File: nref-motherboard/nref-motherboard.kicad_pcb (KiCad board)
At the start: 6 copper layers, 122.6 x 80 mm, 204 parts, among them J1 POWSW, J10 DISP, J11 BAT1, J12 BAT2, J13 SYSCTL_USB, J16 Conn_01x10_Pin, J17 Conn_01x10_Pin, J18 Conn_01x20, J19 SER, J2 Conn_01x12_Pin, J4 1-2199230-6, J5 SYSCTL, J6 USB_INT1, J7 PWR, J8 Conn_01x12_Pin, J9 Conn_01x14_Pin, Q1 NTMFD6H840NL, Q2 NTMFD6H840NL, SW2 RESET, SW4 SW_DIP_x08, U1 reform2-som-connector, U10 BQ25756RRVR, U11 LM62460, U2 74HC573, U3 MAX1837EUT33+T, U5 LM62460, U7 USB2514B_Bi, U8 RP2040, U9 W25Q32JVSS, Y1 12MHz 18pF, Y2 24MHz

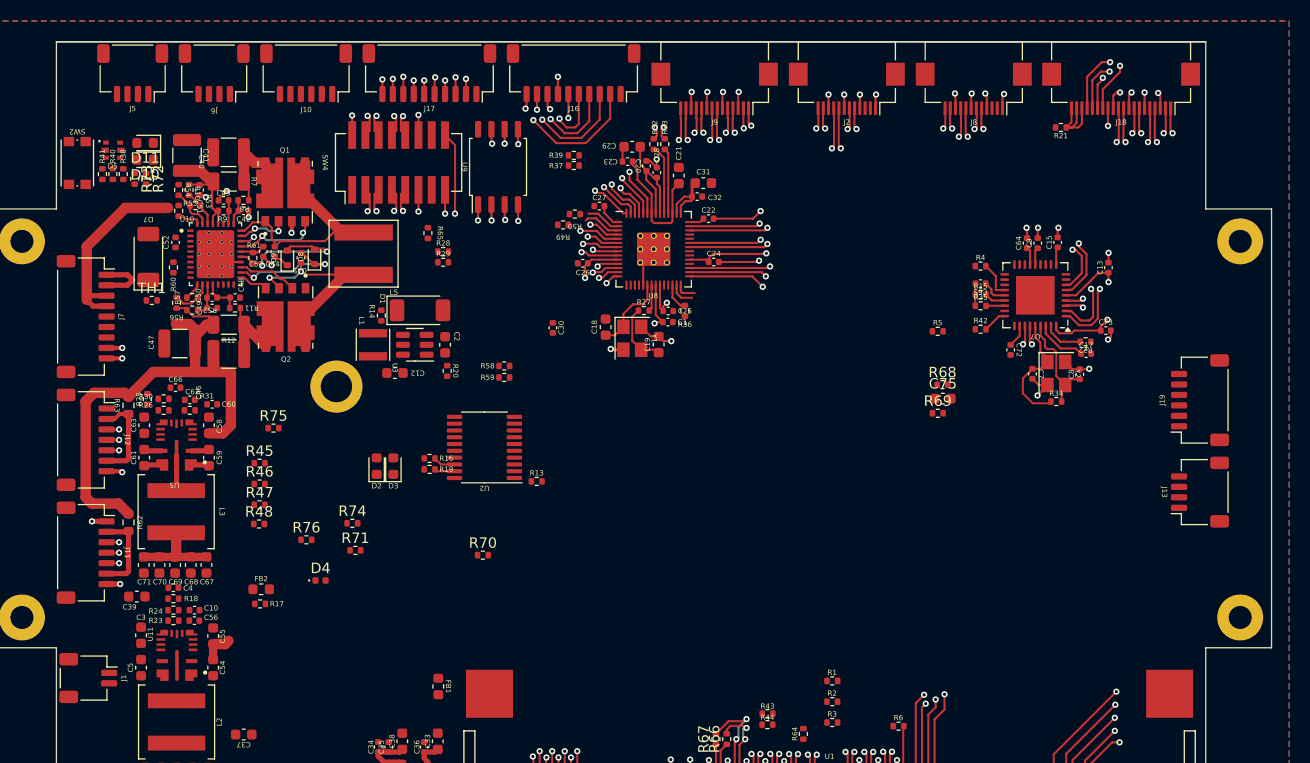
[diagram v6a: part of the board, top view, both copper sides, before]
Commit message: mb: swap some intersecting connectors; more routing
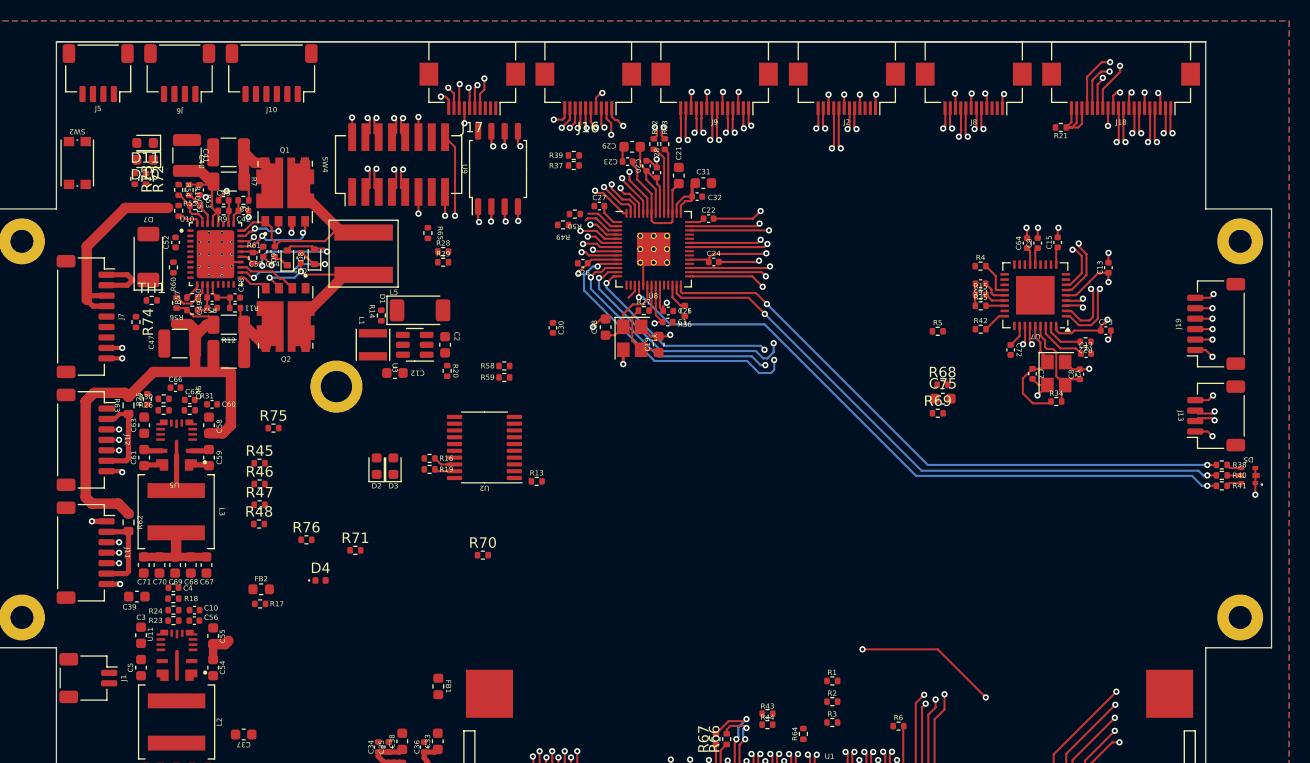
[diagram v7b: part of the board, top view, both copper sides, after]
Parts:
- J16, J17: footprint Connector_JST:JST_SH_SM10B-SRSS-TB_1x10-1MP_P1.00mm_Horizontal -> Connector_FFC-FPC:Hirose_FH12-10S-0.5SH_1x10-1MP_P0.50mm_Horizontal
- moved D5 113.0 mm to (144.1, 141.5), turned to 180 degrees
- moved R41 111.2 mm to (141.5, 142.5), turned to 0 degrees
- moved R40 110.0 mm to (141.5, 141.5), turned to 0 degrees
- moved R38 108.8 mm to (141.5, 140.5), turned to 0 degrees
- moved R74 28.3 mm to (37.6, 126.8), turned to -90 degrees
- moved J19 7.46 mm to (141.0, 127.0)
- moved J13 7.46 mm to (141.0, 135.8)
- moved J17 4.37 mm to (69.8, 104.5)
- moved J6 3.30 mm to (41.8, 103.0)
- moved J10 3.30 mm to (50.6, 103.0)
- moved J5 3.30 mm to (34.0, 103.0)
- moved J16 2.05 mm to (80.9, 104.5)
- moved SW4 0.20 mm to (62.8, 111.8)
- moved U9 0.20 mm to (72.3, 112.2)
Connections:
- J16 pad 2: SD_D0 -> SD_DET
- J16 pad 3: SD_D1 -> SD_CLK
- J16 pad 4: SD_D2 -> GND
- J16 pad 5: SD_D3 -> SD_CMD
- J16 pad 6: SD_CMD -> SD_D3
- J16 pad 7: GND -> SD_D2
- J16 pad 8: SD_CLK -> SD_D1
- J16 pad 9: SD_DET -> SD_D0
- U1 pad 30: RP_UART2_RX -> unconnected-(U1-UART3_TXD-Pad30)
- U1 pad 32: RP_UART2_TX -> unconnected-(U1-UART3_RXD-Pad32)
- U8 pad 15: RP_UART2_TX -> unconnected-(U8-GPIO12-Pad15)
- U8 pad 16: RP_UART2_RX -> unconnected-(U8-GPIO13-Pad16)
- U8 pad 35: 1V1_ENABLE -> unconnected-(U8-GPIO23-Pad35)
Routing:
- net IMX_WAKE: track 9.47 -> 76.8 mm, vias 2 -> 4
- net LPC_MOSI: track 14.2 -> 78.5 mm, vias 2 -> 3
- net Net-(U8-GPIO15): track 0.00 -> 63.9 mm, vias 0 -> 2
- net LPC_SCK: track 14.3 -> 76.0 mm, vias 2 -> 3
- net LPC_SS0: track 14.8 -> 74.8 mm, vias 2 -> 3
- net LPC_MISO: track 14.2 -> 71.9 mm, vias 2 -> 3
- net Net-(U8-GPIO16): track 2.44 -> 59.7 mm, vias 0 -> 2
- net Net-(U8-GPIO17): track 2.02 -> 58.8 mm, vias 0 -> 2
- net SD_D0: track 74.7 -> 65.4 mm
- net GND: track 173.8 -> 182.6 mm, vias 94 -> 98
- net SD_D1: track 72.4 -> 65.4 mm
- net SD_D2: track 70.4 -> 65.3 mm
- net DAC_MCLK: track 136.4 -> 131.5 mm
- net DAC_BCLK: track 142.0 -> 137.1 mm
- net SD_DET: track 71.0 -> 66.2 mm
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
